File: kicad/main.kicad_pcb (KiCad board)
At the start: 2 copper layers, 99.7 x 87.6 mm, 41 parts, among them J1 Jack-DC, J2 LCD, J3 VIA_A, J4 VIA_B, SW1 Step, SW2 Reset, X1 1 MHz

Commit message: Update V8 schematics, move I/O to $Dxxx
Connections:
- IO1 pad 5: A_{12} -> Net-(ADDR1-Pad3)
- IO1 pad 6: RAM~{EN} -> A_{12}

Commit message: V9 & GAL stuff
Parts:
- added J3: Addr, Connector_PinHeader_2.54mm:PinHeader_1x08_P2.54mm_Vertical, F.Cu at (108.6, 66.7)
- added J4: IO~{EN}_{[2..7]}, Connector_PinHeader_2.54mm:PinHeader_2x03_P2.54mm_Vertical, F.Cu at (117.5, 81.9)
- added J5: Data, Connector_PinHeader_2.54mm:PinHeader_1x08_P2.54mm_Vertical, F.Cu at (116.2, 66.7)
- added J6: Control, Connector_PinHeader_2.54mm:PinHeader_2x05_P2.54mm_Vertical, F.Cu at (109.9, 84.5)
- moved J7 33.0 mm to (109.9, 41.3)
- moved J8 7.61 mm to (117.5, 41.3)
- renumbered C6 to C4, C4 to C5, C5 to C6, J3 to J7, J4 to J8
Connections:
- C3 pad 1: +5V -> GND
- C3 pad 2: GND -> +5V
- C4 pad 1: +5V -> GND
- C4 pad 2: GND -> +5V
- IO1 pad 10: unconnected-(IO1-Pad10) -> IO~{EN}_{5}
- IO1 pad 11: unconnected-(IO1-Pad11) -> IO~{EN}_{4}
- IO1 pad 12: unconnected-(IO1-Pad12) -> IO~{EN}_{3}
- IO1 pad 13: unconnected-(IO1-Pad13) -> IO~{EN}_{2}
- IO1 pad 7: unconnected-(IO1-Pad7) -> IO~{EN}_{7}
- IO1 pad 9: unconnected-(IO1-Pad9) -> IO~{EN}_{6}
- J7 pad 13: GND -> +5V
- J7 pad 14: +5V -> GND
- J8 pad 13: GND -> +5V
- J8 pad 14: +5V -> GND
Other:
- board text added: "v0.9"
- board text removed: "v0.8"

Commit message: Add standoffs, update V9 render
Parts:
- C3: value 10uF -> 0,1uF

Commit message: Add Traco Power TSR 1-2450
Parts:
- REG1: footprint Package_TO_SOT_THT:TO-220-3_Vertical -> kicad:CONV_TSR_1-2450
- moved C2 9.92 mm to (42.5, 20.3), turned to 180 degrees
- moved REG1 3.87 mm to (40.6, 27.9)
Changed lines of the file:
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@@
     )
   )
-  (footprint "Package_TO_SOT_THT:TO-220-3_Vertical" (layer "F.Cu")
-    (at 42.855 31.115 90)
-    (descr "TO-220-3, Vertical, RM 2.54mm, see https://www.vishay.com/docs/66542/to-220-1.pdf")
-    (tags "TO-220-3 Vertical RM 2.54mm")
+  (footprint "kicad:CONV_TSR_1-2450" (layer "F.Cu")
+    (at 40.64 27.94 90)
     (property "Sheetfile" "main.kicad_sch")
     (property "Sheetname" "")
     (property "Vendor" "Traco Power")
     (attr through_hole)
-    (fp_text reference "REG1" (at 8.875 -0.945) (layer "F.SilkS")
+    (fp_text reference "REG1" (at -3.81 5.08 90) (layer "F.SilkS")
       (effects (font (size 1 1) (thickness 0.15)))
     )
-    (fp_text value "TSC 1-2450" (at 2.54 2.5 90) (layer "F.Fab")
+    (fp_text value "TSC 1-2450" (at -0.635 -2.54 90) (layer "F.Fab")
       (effects (font (size 1 1) (thickness 0.15)))
     )
-    (fp_line (start 0.69 -3.27) (end 0.69 -1.76) (layer "F.SilkS") (width 0.12))
-    (fp_line (start -2.58 1.371) (end 7.66 1.371) (layer "F.SilkS") (width 0.12))
-    (fp_line (start -2.58 -3.27) (end -2.58 1.371) (layer "F.SilkS") (width 0.12))
-    (fp_line (start 4.391 -3.27) (end 4.391 -1.76) (layer "F.SilkS") (width 0.12))
-    (fp_line (start 7.66 -3.27) (end 7.66 1.371) (layer "F.SilkS") (width 0.12))
-    (fp_line (start -2.58 -1.76) (end 7.66 -1.76) (layer "F.SilkS") (width 0.12))
-    (fp_line (start -2.58 -3.27) (end 7.66 -3.27) (layer "F.SilkS") (width 0.12))
-    (fp_line (start 7.79 -3.4) (end -2.71 -3.4) (layer "F.CrtYd") (width 0.05))
-    (fp_line (start 7.79 1.51) (end 7.79 -3.4) (layer "F.CrtYd") (width 0.05))
-    (fp_line (start -2.71 -3.4) (end -2.71 1.51) (layer "F.CrtYd") (width 0.05))
-    (fp_line (start -2.71 1.51) (end 7.79 1.51) (layer "F.CrtYd") (width 0.05))
-    (fp_line (start -2.46 -1.88) (end 7.54 -1.88) (layer "F.Fab") (width 0.1))
-    (fp_line (start 7.54 1.25) (end 7.54 -3.15) (layer "F.Fab") (width 0.1))
-    (fp_line (start 4.39 -3.15) (end 4.39 -1.88) (layer "F.Fab") (width 0.1))
-    (fp_line (start 0.69 -3.15) (end 0.69 -1.88) (layer "F.Fab") (width 0.1))
-    (fp_line (start -2.46 -3.15) (end -2.46 1.25) (layer "F.Fab") (width 0.1))
-    (fp_line (start -2.46 1.25) (end 7.54 1.25) (layer "F.Fab") (width 0.1))
-    (fp_line (start 7.54 -3.15) (end -2.46 -3.15) (layer "F.Fab") (width 0.1))
-    (pad "1" thru_hole rect (at 0 0 90) (size 1.905 2) (drill 1.1) (layers *.Cu *.Mask)
+    (fp_line (start 5.85 -3.75) (end 5.85 3.75) (layer "F.SilkS") (width 0.127))
+    (fp_line (start -5.85 3.75) (end 5.85 3.75) (layer "F.SilkS") (width 0.127))
+    (fp_line (start -5.85 -3.75) (end 5.85 -3.75) (layer "F.SilkS") (width 0.127))
+    (fp_line (start -5.85 3.75) (end -5.85 -3.75) (layer "F.SilkS") (width 0.127))
+    (fp_circle (center -6.55 1.75) (end -6.45 1.75) (layer "F.SilkS") (width 0.2) (fill none))
+    (fp_line (start 6.1 4) (end 6.1 -4) (layer "F.CrtYd") (width 0.05))
+    (fp_line (start -6.1 -4) (end -6.1 4) (layer "F.CrtYd") (width 0.05))
+    (fp_line (start -6.1 4) (end 6.1 4) (layer "F.CrtYd") (width 0.05))
+    (fp_line (start 6.1 -4) (end -6.1 -4) (layer "F.CrtYd") (width 0.05))
+    (fp_line (start 5.85 -3.75) (end 5.85 3.75) (layer "F.Fab") (width 0.127))
+    (fp_line (start 5.85 3.75) (end -5.85 3.75) (layer "F.Fab") (width 0.127))
+    (fp_line (start -5.85 -3.75) (end 5.85 -3.75) (layer "F.Fab") (width 0.127))
+    (fp_line (start -5.85 3.75) (end -5.85 -3.75) (layer "F.Fab") (width 0.127))
+    (fp_circle (center -6.55 1.75) (end -6.45 1.75) (layer "F.Fab") (width 0.2) (fill none))
+    (pad "1" thru_hole rect locked (at -2.54 1.75 90) (size 1.358 1.358) (drill 0.85) (layers *.Cu *.Mask)
       (net 52 "/PWR_UNREG") (pinfunction "VI") (pintype "power_in"))
-    (pad "2" thru_hole oval (at 2.54 0 90) (size 1.905 2) (drill 1.1) (layers *.Cu *.Mask)
+    (pad "2" thru_hole circle locked (at 0 1.75 90) (size 1.358 1.358) (drill 0.85) (layers *.Cu *.Mask)
       (net 1 "GND") (pinfunction "GND") (pintype "power_in"))
-    (pad "3" thru_hole oval (at 5.08 0 90) (size 1.905 2) (drill 1.1) (layers *.Cu *.Mask)
+    (pad "3" thru_hole circle locked (at 2.54 1.75 90) (size 1.358 1.358) (drill 0.85) (layers *.Cu *.Mask)
       (net 3 "+5V") (pinfunction "VO") (pintype "power_out"))
-    (model "${KICAD6_3DMODEL_DIR}/Package_TO_SOT_THT.3dshapes/TO-220-3_Vertical.wrl"
-      (offset (xyz 0 0 0))
+    (model "${KIPRJMOD}/TSR_1-2450.step"
+      (offset (xyz 0 0 5.5))
       (scale (xyz 1 1 1))
-      (rotate (xyz 0 0 0))
+      (rotate (xyz -90 0 0))
     )
   )
@@
   )
   (footprint "Capacitor_THT:C_Disc_D3.0mm_W2.0mm_P2.50mm" (layer "F.Cu")
-    (at 38.1 29.19 90)
+    (at 42.545 20.32 180)
     (descr "C, Disc series, Radial, pin pitch=2.50mm, , diameter*width=3*2mm^2, Capacitor")
     (tags "C Disc series Radial pin pitch 2.50mm  diameter 3mm width 2mm Capacitor")
@@
     (property "Sheetname" "")
     (attr through_hole)
-    (fp_text reference "C2" (at -2.555 0 90) (layer "F.SilkS")
-      (effects (font (size 1 1) (thickness 0.15)))
+    (fp_text reference "C2" (at 4.445 0 90) (layer "F.SilkS")
+      (effects (font (size 0.8 0.8) (thickness 0.15)))
     )
-    (fp_text value "10uF" (at 5.7 0 90) (layer "F.Fab")
-      (effects (font (size 1 1) (thickness 0.15)))
+    (fp_text value "10uF" (at 1.27 1.905 180) (layer "F.Fab")
+      (effects (font (size 0.8 0.8) (thickness 0.15)))
     )
     (fp_line (start -0.37 -1.12) (end -0.37 -1.055) (layer "F.SilkS") (width 0.12))
@@
     (fp_line (start 2.75 1) (end 2.75 -1) (layer "F.Fab") (width 0.1))
     (fp_line (start -0.25 1) (end 2.75 1) (layer "F.Fab") (width 0.1))
-    (pad "1" thru_hole circle (at 0 0 90) (size 1.6 1.6) (drill 0.8) (layers *.Cu *.Mask)
+    (pad "1" thru_hole circle (at 0 0 180) (size 1.6 1.6) (drill 0.8) (layers *.Cu *.Mask)
       (net 52 "/PWR_UNREG") (pintype "passive"))
-    (pad "2" thru_hole circle (at 2.5 0 90) (size 1.6 1.6) (drill 0.8) (layers *.Cu *.Mask)
+    (pad "2" thru_hole circle (at 2.5 0 180) (size 1.6 1.6) (drill 0.8) (layers *.Cu *.Mask)
       (net 1 "GND") (pintype "passive"))
     (model "${KICAD6_3DMODEL_DIR}/Capacitor_THT.3dshapes/C_Disc_D3.0mm_W2.0mm_P2.50mm.wrl"

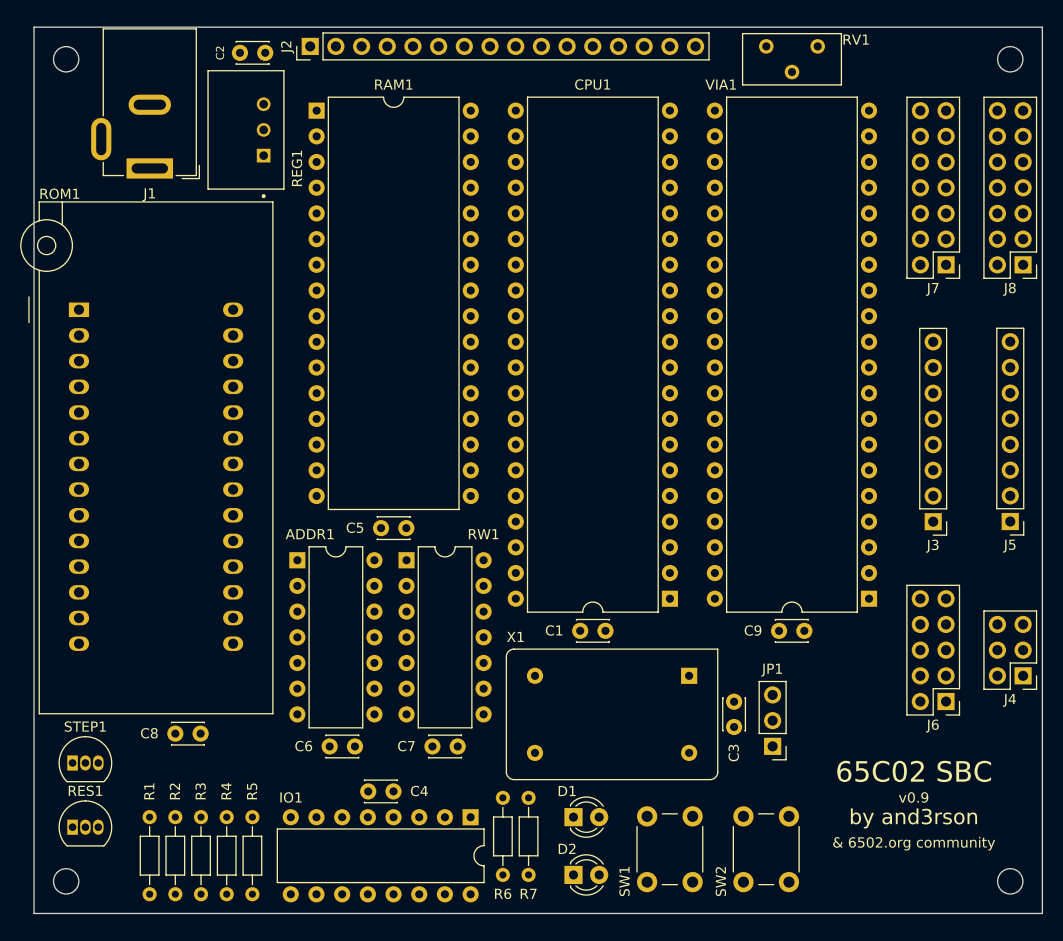
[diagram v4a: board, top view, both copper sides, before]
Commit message: Update ROM code to be runnable in sim65, increase PCB spacing at borders
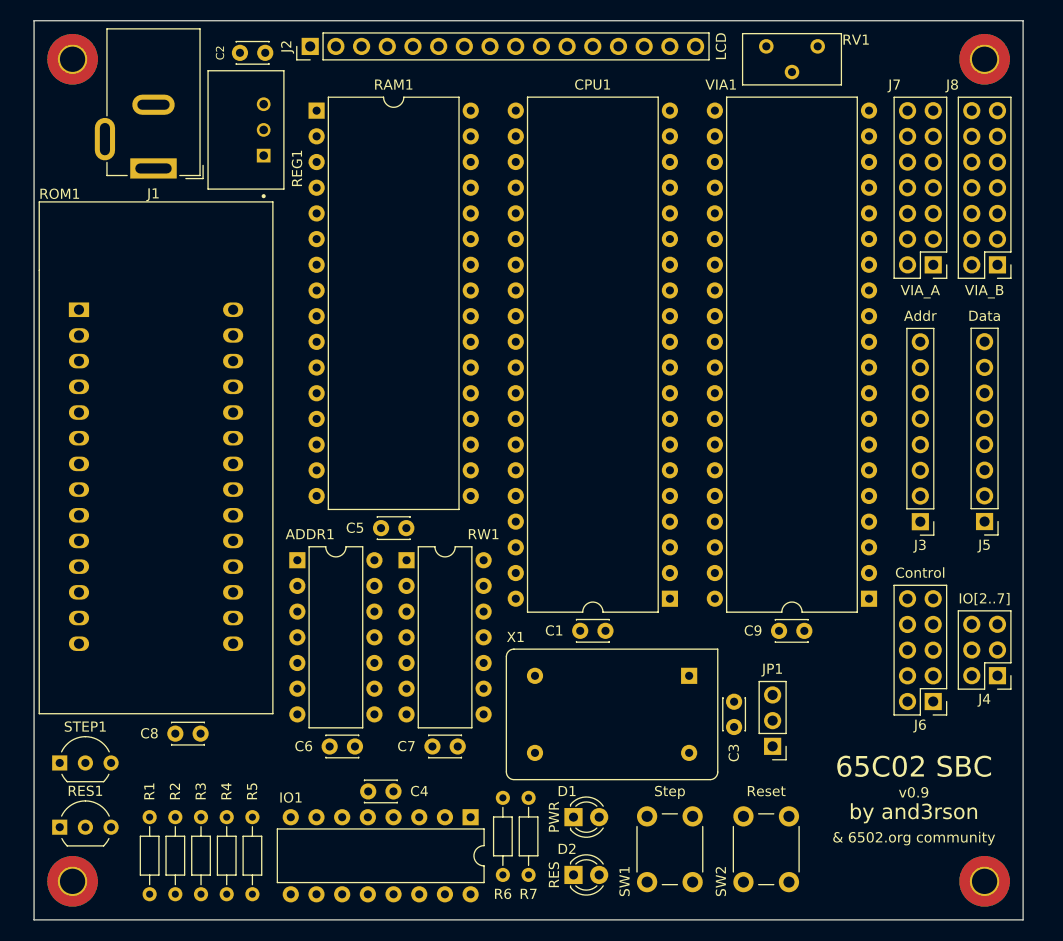
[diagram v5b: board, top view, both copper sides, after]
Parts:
- removed the REF** at (22.9, 102.2)
- removed the REF** at (22.9, 21.0)
- removed the REF** at (116.2, 102.2)
- removed the REF** at (116.2, 21.0)
- added REF**: MountingHole_2.5mm_Pad_TopBottom, MountingHole:MountingHole_2.5mm_Pad_TopBottom, F.Cu at (23.5, 102.2)
- added REF**: MountingHole_2.5mm_Pad_TopBottom, MountingHole:MountingHole_2.5mm_Pad_TopBottom, F.Cu at (23.5, 21.0)
- added REF**: MountingHole_2.5mm_Pad_TopBottom, MountingHole:MountingHole_2.5mm_Pad_TopBottom, F.Cu at (113.7, 102.2)
- added REF**: MountingHole_2.5mm_Pad_TopBottom, MountingHole:MountingHole_2.5mm_Pad_TopBottom, F.Cu at (113.7, 21.0)
- RES1, STEP1: footprint Package_TO_SOT_THT:TO-92_Inline -> Package_TO_SOT_THT:TO-92_Inline_Wide
- moved J5 2.54 mm to (113.7, 66.7)
- moved J4 2.54 mm to (114.9, 81.9)
- moved J8 2.53 mm to (114.9, 41.3)
- moved J6 1.27 mm to (108.6, 84.5)
- moved RES1 1.27 mm to (22.2, 96.9)
- moved STEP1 1.27 mm to (22.2, 90.5)
- moved J3 1.27 mm to (107.3, 66.7)
- moved J7 1.27 mm to (108.6, 41.3)
- moved J1 0.37 mm to (31.5, 31.8)
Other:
- board size 99.7 x 87.6 mm -> 97.8 x 88.9 mm
- board text added: "Addr"
- board text added: "Control"
- board text added: "Data"
- board text added: "PWR"
- board text added: "RES"
- board text added: "Reset"
- board text added: "Step"
- board text added: "VIA_A"
- board text added: "VIA_B"

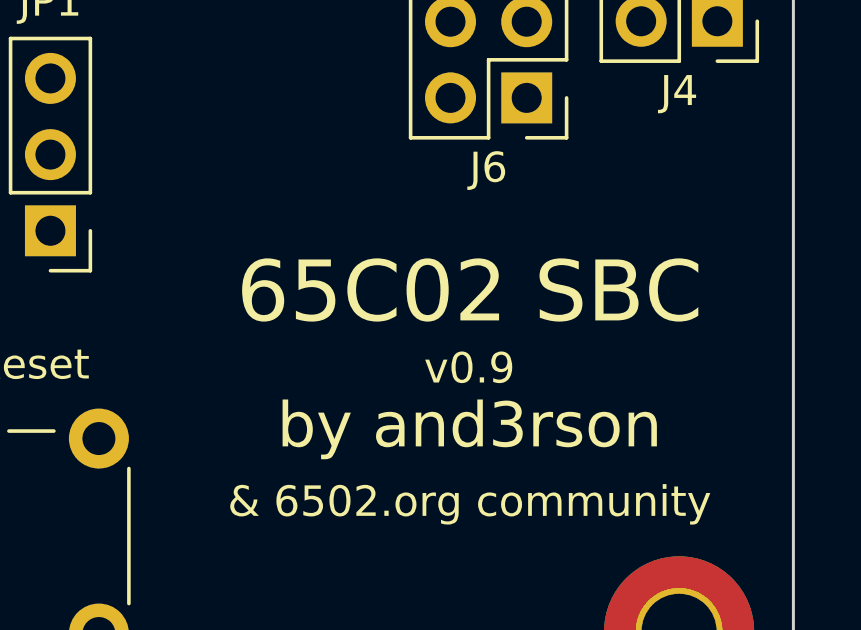
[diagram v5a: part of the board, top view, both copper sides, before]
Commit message: Update PCB wording, remove outer rectangle
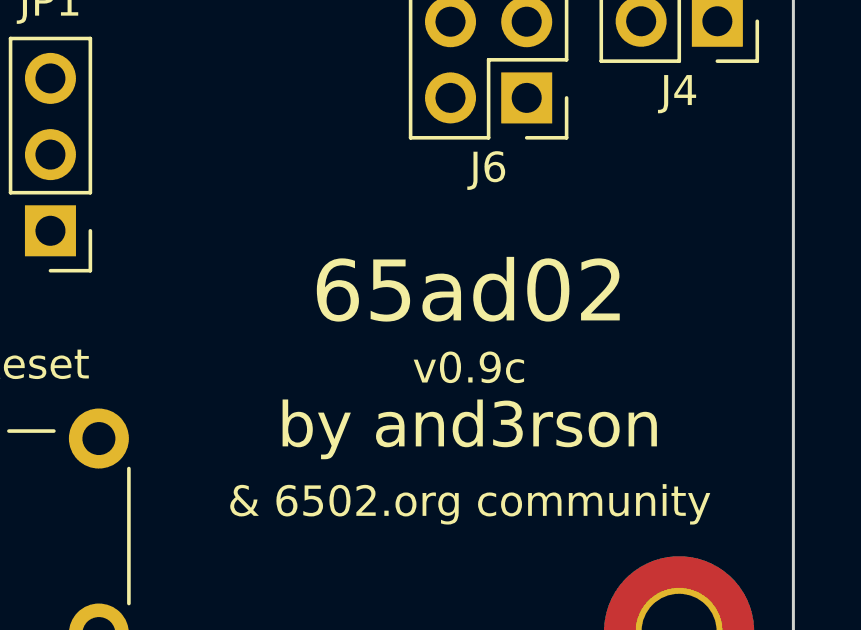
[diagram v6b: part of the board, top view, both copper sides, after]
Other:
- board text added: "65ad02"
- board text added: "v0.9c"
- board text removed: "65C02 SBC"
- board text removed: "v0.9"
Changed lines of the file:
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@@
   )
   (gr_rect (start 19.685 17.145) (end 117.475 106.045) (layer "Edge.Cuts") (width 0.1) (fill none))
-  (gr_text "65C02 SBC" (at 106.68 90.932) (layer "F.SilkS")
+  (gr_text "65ad02" (at 106.68 90.932) (layer "F.SilkS")
     (effects (font (size 2.032 2.032) (thickness 0.3)))
   )
@@
     (effects (font (size 1 1) (thickness 0.15)))
   )
-  (gr_text "v0.9" (at 106.68 93.472) (layer "F.SilkS")
+  (gr_text "v0.9c" (at 106.68 93.472) (layer "F.SilkS")
     (effects (font (size 1.016 1.016) (thickness 0.15875)))
   )

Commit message: V11
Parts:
- added C6: 0.1uF, Capacitor_THT:C_Disc_D3.0mm_W2.0mm_P2.50mm, F.Cu at (47.6, 92.1)
- added IO2: 74HC00, Package_DIP:DIP-14_W7.62mm, F.Cu at (47.6, 102.2)
- moved JP1 53.8 mm to (40.6, 102.2), turned to -90 degrees
- moved C10 49.7 mm to (97.8, 27.9), turned to 180 degrees
- moved C9 41.0 mm to (45.1, 48.2), turned to 90 degrees
- moved C7 39.6 mm to (58.4, 27.9), turned to 180 degrees
- moved R7 37.0 mm to (102.9, 80.0)
- moved R6 37.0 mm to (100.3, 80.0)
- moved C2 22.3 mm to (79.4, 55.9), turned to 180 degrees
- moved C3 22.3 mm to (47.6, 66.7)
- moved RW1 21.0 mm to (47.6, 89.5), turned to 90 degrees
- moved C8 16.9 mm to (47.6, 79.4), turned to 0 degrees
- moved C4 16.7 mm to (71.1, 88.2), turned to 90 degrees
- moved IO1 14.7 mm to (67.3, 81.9), turned to 0 degrees
- moved D1 14.0 mm to (87.0, 95.9)
- moved D2 14.0 mm to (87.0, 101.6)
- moved X1 11.4 mm to (95.9, 81.9)
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- renumbered C2 to C1, C9 to C10, C1 to C2, C6 to C3, C3 to C5, C5 to C7, C7 to C8, C8 to C9, J7 to J5, J8 to J6, J5 to J7, J6 to J8
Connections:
- C9 pad 1: +5V -> GND
- C9 pad 2: GND -> +5V
- IO1 pad 15: LCD~{EN} -> Net-(IO2-Pad1)
- J2 pad 5: ~{WD} -> R~{W}
- J2 pad 6: LCD~{EN} -> LCDEN
- RW1 pad 10: Ф2 -> R~{W}
- RW1 pad 9: R~{W} -> Ф2
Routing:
- net +5V: track 0.00 -> 50.4 mm
- net GND: track 0.00 -> 14.3 mm
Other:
- board text added: "v0.10"
- board text removed: "v0.9c"
